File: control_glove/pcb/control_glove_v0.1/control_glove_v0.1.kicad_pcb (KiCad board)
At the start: 2 copper layers, 194 x 51 mm, 44 parts, among them J1 Conn_01x04_Female, J2 Conn_01x04_Female, J3 Conn_01x03_Female, J4 Conn_01x03_Female, J5 Conn_01x03_Female, J6 Conn_01x03_Female, J7 Conn_01x04_Female, J8 Conn_01x04_Female, P1 Power_Pins, SW3 SW_Push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

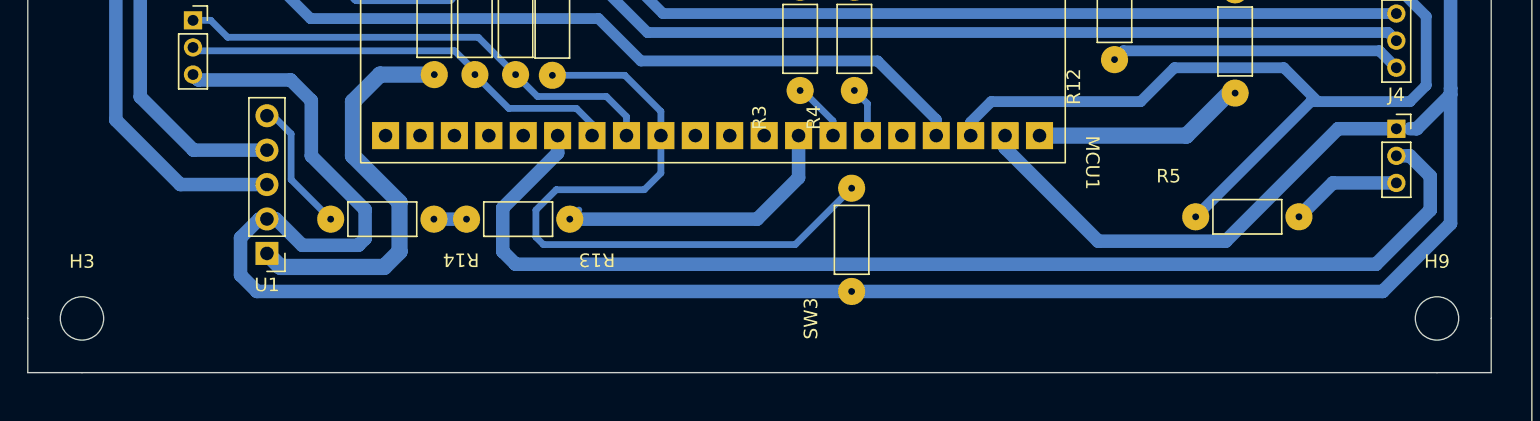
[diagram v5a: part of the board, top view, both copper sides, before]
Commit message: update: Change pcb size to 38 x 100
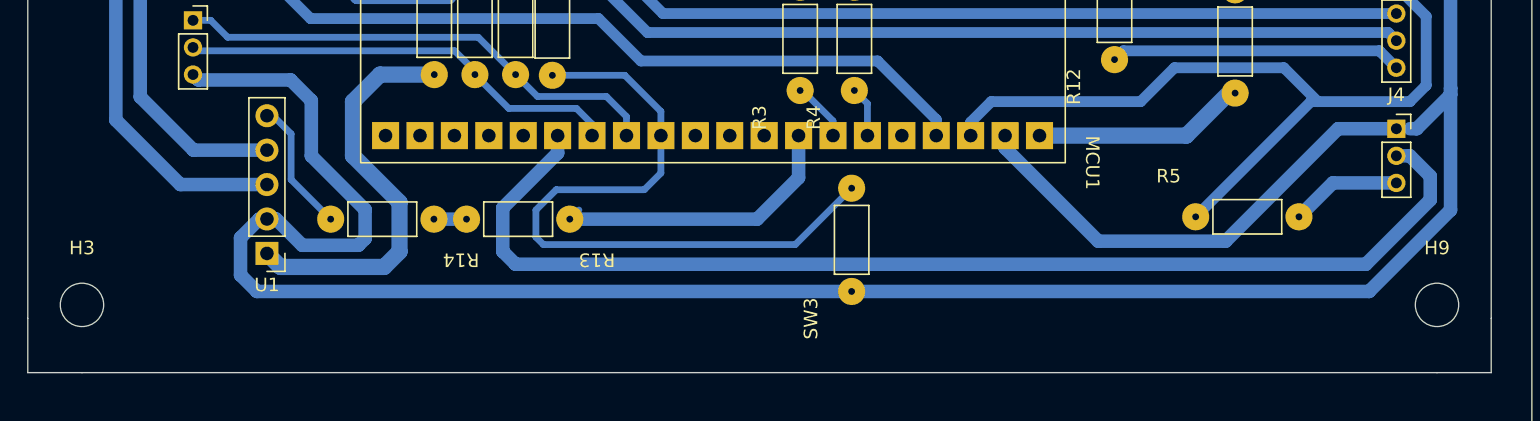
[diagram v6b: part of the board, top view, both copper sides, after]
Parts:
- moved H3 1.00 mm to (20.0, 57.0)
- moved H9 1.00 mm to (120.0, 57.0)
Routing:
- net GND: track 256.2 -> 255.6 mm
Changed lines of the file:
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@@
   )
   (footprint "MountingHole:MountingHole_3.2mm_M3" (layer "F.Cu")
-    (at 20 58)
+    (at 20 57)
     (descr "Mounting Hole 3.2mm, no annular, M3")
     (tags "mounting hole 3.2mm no annular m3")
@@
   )
   (footprint "MountingHole:MountingHole_3.2mm_M3" (layer "F.Cu")
-    (at 120 58)
+    (at 120 57)
     (descr "Mounting Hole 3.2mm, no annular, M3")
     (tags "mounting hole 3.2mm no annular m3")
@@
   (via (at 20 19) (size 3) (drill 2) (layers "F.Cu" "B.Cu") (free) (net 0))
   (via (at 120 19) (size 3) (drill 2) (layers "F.Cu" "B.Cu") (free) (net 0))
-  (via (at 120 58) (size 3) (drill 2) (layers "F.Cu" "B.Cu") (free) (net 0))
-  (via (at 20 58) (size 3) (drill 2) (layers "F.Cu" "B.Cu") (free) (net 0))
+  (via (at 120 57) (size 3) (drill 2) (layers "F.Cu" "B.Cu") (free) (net 0))
+  (via (at 20 57) (size 3) (drill 2) (layers "F.Cu" "B.Cu") (free) (net 0))
   (segment (start 55.10469 44.508049) (end 55.10469 45.79531) (width 1) (layer "B.Cu") (net 1))
-  (segment (start 115.5 54) (end 119.5 50) (width 1) (layer "B.Cu") (net 1))
+  (segment (start 51.054 53.054) (end 52 54) (width 1) (layer "B.Cu") (net 1))
+  (segment (start 119.5 47.5) (end 118 46) (width 1) (layer "B.Cu") (net 1))
   (segment (start 55.10469 45.79531) (end 51.054 49.846) (width 1) (layer "B.Cu") (net 1))
-  (segment (start 119.5 47.5) (end 118 46) (width 1) (layer "B.Cu") (net 1))
-  (segment (start 119.5 50) (end 119.5 47.5) (width 1) (layer "B.Cu") (net 1))
+  (segment (start 51.054 49.846) (end 51.054 53.054) (width 1) (layer "B.Cu") (net 1))
   (segment (start 118 46) (end 117 46) (width 1) (layer "B.Cu") (net 1))
-  (segment (start 51.054 49.846) (end 51.054 53.054) (width 1) (layer "B.Cu") (net 1))
-  (segment (start 52 54) (end 115.5 54) (width 1) (layer "B.Cu") (net 1))
-  (segment (start 51.054 53.054) (end 52 54) (width 1) (layer "B.Cu") (net 1))
+  (segment (start 52 54) (end 114.75 54) (width 1) (layer "B.Cu") (net 1))
+  (segment (start 119.5 49.25) (end 119.5 47.5) (width 1) (layer "B.Cu") (net 1))
+  (segment (start 114.75 54) (end 119.5 49.25) (width 1) (layer "B.Cu") (net 1))
+  (segment (start 33.09 50.66) (end 33.65 50.66) (width 1) (layer "B.Cu") (net 2))
   (segment (start 33.65 50.66) (end 34.314679 50.66) (width 1) (layer "B.Cu") (net 2))
+  (segment (start 112.7 44) (end 117 44) (width 1) (layer "B.Cu") (net 2))
+  (segment (start 114.99 56.01) (end 32.91 56.01) (width 1) (layer "B.Cu") (net 2))
   (segment (start 31.7 54.8) (end 31.7 52.05) (width 1) (layer "B.Cu") (net 2))
-  (segment (start 112.7 44) (end 117 44) (width 1) (layer "B.Cu") (net 2))
+  (segment (start 121 50) (end 114.99 56.01) (width 1) (layer "B.Cu") (net 2))
   (segment (start 84.55 18.13) (end 94.23 18.13) (width 1) (layer "B.Cu") (net 2))
   (segment (start 102.1 28.5) (end 105.6 28.5) (width 1) (layer "B.Cu") (net 2))
-  (segment (start 33.09 50.66) (end 33.65 50.66) (width 1) (layer "B.Cu") (net 2))
   (segment (start 94.23 18.13) (end 101 24.9) (width 1) (layer "B.Cu") (net 2))
   (segment (start 82.83469 25.928049) (end 85.83469 25.928049) (width 1) (layer "B.Cu") (net 2))
   (segment (start 118.5 44) (end 118 44) (width 1) (layer "B.Cu") (net 2))
+  (segment (start 31.7 52.05) (end 33.09 50.66) (width 1) (layer "B.Cu") (net 2))
   (segment (start 104.4 52.3) (end 112.7 44) (width 1) (layer "B.Cu") (net 2))
   (segment (start 40.894 52.106) (end 40.894 49.971478) (width 1) (layer "B.Cu") (net 2))
@@
   (segment (start 101 27.4) (end 102.1 28.5) (width 1) (layer "B.Cu") (net 2))
   (segment (start 36.925 46.002478) (end 36.925 41.925) (width 1) (layer "B.Cu") (net 2))
-  (segment (start 121 51) (end 115.99 56.01) (width 1) (layer "B.Cu") (net 2))
   (segment (start 117.954594 27.5) (end 121 30.545406) (width 1) (layer "B.Cu") (net 2))
   (segment (start 36.254679 52.6) (end 40.4 52.6) (width 1) (layer "B.Cu") (net 2))
   (segment (start 80.731641 22.1) (end 80.80969 22.178049) (width 0.8) (layer "B.Cu") (net 2))
+  (segment (start 121 41) (end 121 50) (width 1) (layer "B.Cu") (net 2))
   (segment (start 80.80969 22.178049) (end 80.80969 23.903049) (width 1) (layer "B.Cu") (net 2))
   (segment (start 88.12469 45.42469) (end 95 52.3) (width 1) (layer "B.Cu") (net 2))
   (segment (start 28.594 40.4) (end 28.194 40) (width 1) (layer "B.Cu") (net 2))
-  (segment (start 31.7 52.05) (end 33.09 50.66) (width 1) (layer "B.Cu") (net 2))
   (segment (start 34.314679 50.66) (end 36.254679 52.6) (width 1) (layer "B.Cu") (net 2))
   (segment (start 80.80969 21.87031) (end 84.55 18.13) (width 1) (layer "B.Cu") (net 2))
-  (segment (start 121 41) (end 121 51) (width 1) (layer "B.Cu") (net 2))
   (segment (start 121 41) (end 121 41.5) (width 1) (layer "B.Cu") (net 2))
   (segment (start 40.894 49.971478) (end 36.925 46.002478) (width 1) (layer "B.Cu") (net 2))
@@
   (segment (start 88.08469 23.678049) (end 88.08469 22.203049) (width 1) (layer "B.Cu") (net 2))
   (segment (start 117 27.5) (end 112.01 27.5) (width 1) (layer "B.Cu") (net 2))
-  (segment (start 32.91 56.01) (end 31.7 54.8) (width 1) (layer "B.Cu") (net 2))
   (segment (start 35.4 40.4) (end 28.594 40.4) (width 1) (layer "B.Cu") (net 2))
   (segment (start 76.065 22.1) (end 80.731641 22.1) (width 0.8) (layer "B.Cu") (net 2))
   (segment (start 40.4 52.6) (end 40.894 52.106) (width 1) (layer "B.Cu") (net 2))
   (segment (start 121 41.5) (end 118.5 44) (width 1) (layer "B.Cu") (net 2))
-  (segment (start 115.99 56.01) (end 32.91 56.01) (width 1) (layer "B.Cu") (net 2))
+  (segment (start 32.91 56.01) (end 31.7 54.8) (width 1) (layer "B.Cu") (net 2))
   (segment (start 80.80969 23.903049) (end 82.83469 25.928049) (width 1) (layer "B.Cu") (net 2))
   (segment (start 112.01 27.5) (end 110.81 26.3) (width 1) (layer "B.Cu") (net 2))

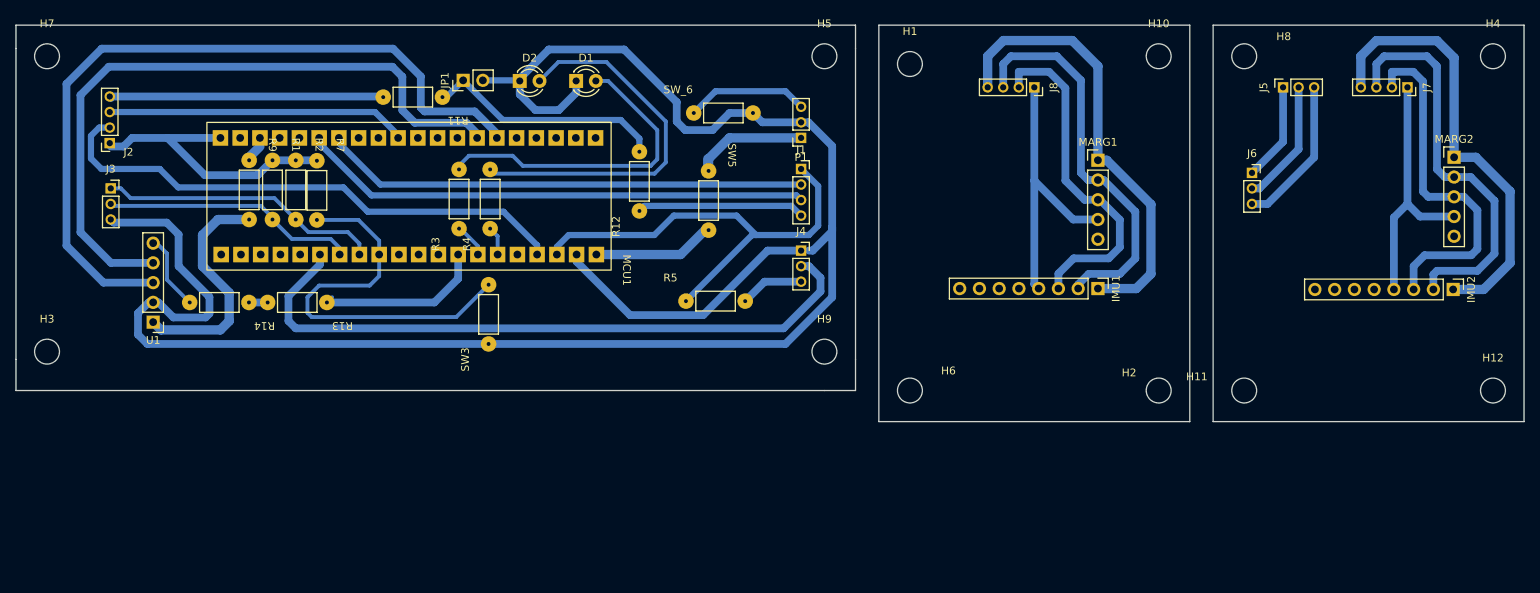
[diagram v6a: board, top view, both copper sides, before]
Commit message: update: Add .asm files
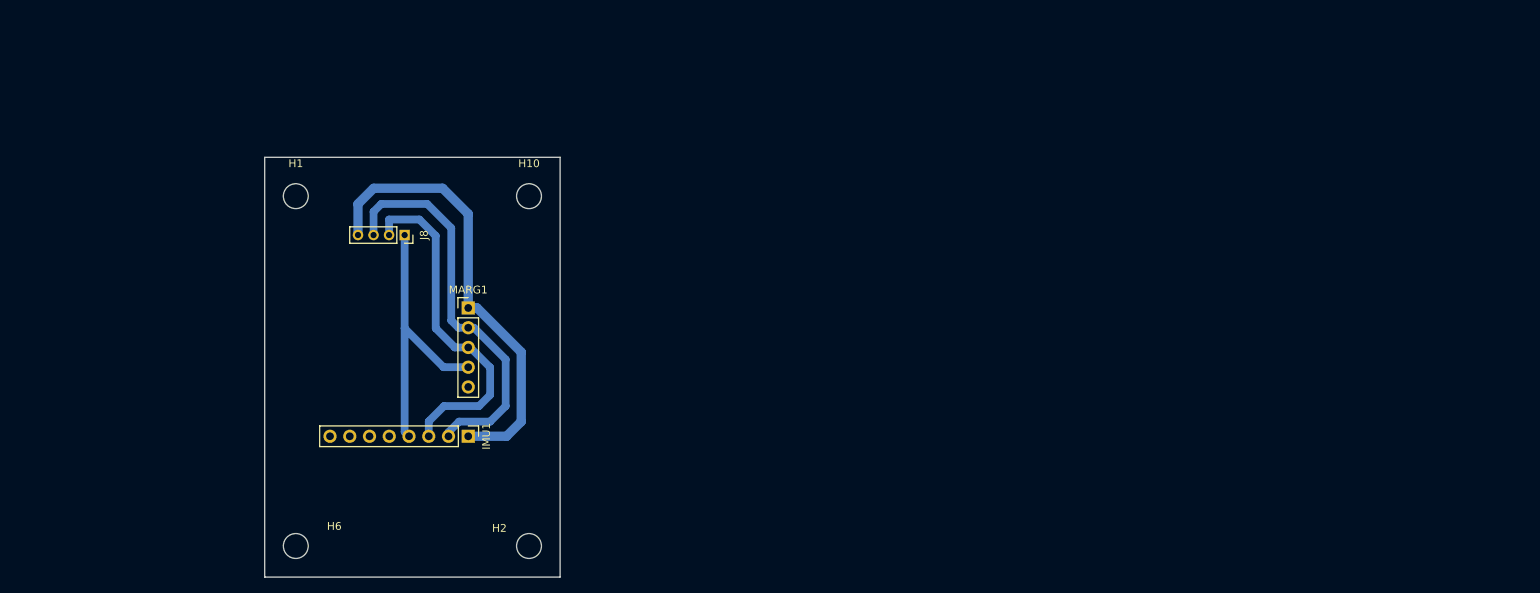
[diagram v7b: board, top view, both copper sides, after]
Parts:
- removed D1, D2: LED, LED_THT:LED_D3.0mm
- removed H11, H12, H3, H4, H5, H7, H8, H9: MountingHole, MountingHole:MountingHole_3.2mm_M3
- removed IMU2: GY-521, Connector_PinHeader_2.54mm:PinHeader_1x08_P2.54mm_Vertical
- removed J1, J2, J7: Conn_01x04_Female, Connector_PinSocket_2.00mm:PinSocket_1x04_P2.00mm_Vertical
- removed J3, J4, J5, J6: Conn_01x03_Female, Connector_PinSocket_2.00mm:PinSocket_1x03_P2.00mm_Vertical
- removed JP1: Jumper_2_Bridged, Connector_PinHeader_2.54mm:PinHeader_1x02_P2.54mm_Vertical
- removed MARG2: HMC5883L, Connector_PinHeader_2.54mm:PinHeader_1x05_P2.54mm_Vertical
- removed MCU1: MiniSTM32F4x1, hieu:stm32f4_board
- removed P1: Power_Pins, Connector_PinSocket_2.00mm:PinSocket_1x03_P2.00mm_Vertical
- removed R1, R2, R7: 1K, hieu:resistor
- removed R11, R12, R13, R14, R9: 0, hieu:resistor
- removed R3, R4: 300, hieu:resistor
- removed R5: 330, hieu:resistor
- removed SW3, SW_6: SW_Push, hieu:resistor
- removed SW5: SW_DIP_x01, hieu:resistor
- removed U1: UART-RF433, Connector_PinHeader_2.54mm:PinHeader_1x05_P2.54mm_Vertical
- moved H2 83.4 mm to (82.0, 82.0)
- moved IMU1 83.2 mm to (74.2, 67.9)
- moved J8 83.2 mm to (66.0, 42.0)
- moved MARG1 83.2 mm to (74.2, 51.4)
- moved H10 83.0 mm to (82.0, 37.0)
- moved H6 81.5 mm to (52.0, 82.0)
- moved H1 80.8 mm to (52.0, 37.0)
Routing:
- net GND: track 255.6 -> 0.00 mm
- net TX: track 98.6 -> 0.00 mm
- net RX: track 87.8 -> 0.00 mm
- net RV1: track 85.9 -> 0.00 mm
- net SCL2: track 69.0 -> 0.00 mm
- net SDA1: track 65.7 -> 0.00 mm
- net SCL1: track 62.3 -> 0.00 mm
- net 3.3V-SHOULDER: track 58.7 -> 0.00 mm
- net Net-(IMU2-Pad1): track 57.5 -> 0.00 mm
- net Net-(IMU2-Pad2): track 51.8 -> 0.00 mm
- net SW3: track 51.5 -> 0.00 mm
- net Net-(D2-Pad2): track 49.1 -> 0.00 mm
- net Net-(IMU2-Pad3): track 45.8 -> 0.00 mm
- net Net-(D1-Pad2): track 41.2 -> 0.00 mm
- net SDA2: track 38.7 -> 0.00 mm
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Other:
- board size 194 x 51 mm -> 38 x 54 mm
